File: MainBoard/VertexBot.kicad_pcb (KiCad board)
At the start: 2 copper layers, 115.6 x 107.8 mm, 68 parts, among them J2 I2C Extension, J3 Left Motor, J4 694106301002, J5 Right Motor, J6 Led Strip, Q1 BSS138, Q2 BSS138, Q3 BSS138, SW1 SW_SPST, U10 MAX4466 (LEFT), U11 MAX4466 (RIGHT), U12 ESP32-S3-CAM-B, U13 ESP32-S3-CAM-A, U14 MAX98357A, U2 DRV8830DGQR, U3 S13V30F5, U4 DRV8830DGQR, U5 INMP441, U6 0.96 INCH OLED, U7 DRV5033AJxLPG, U8 DRV5033AJxLPG, U9 MPU 6050

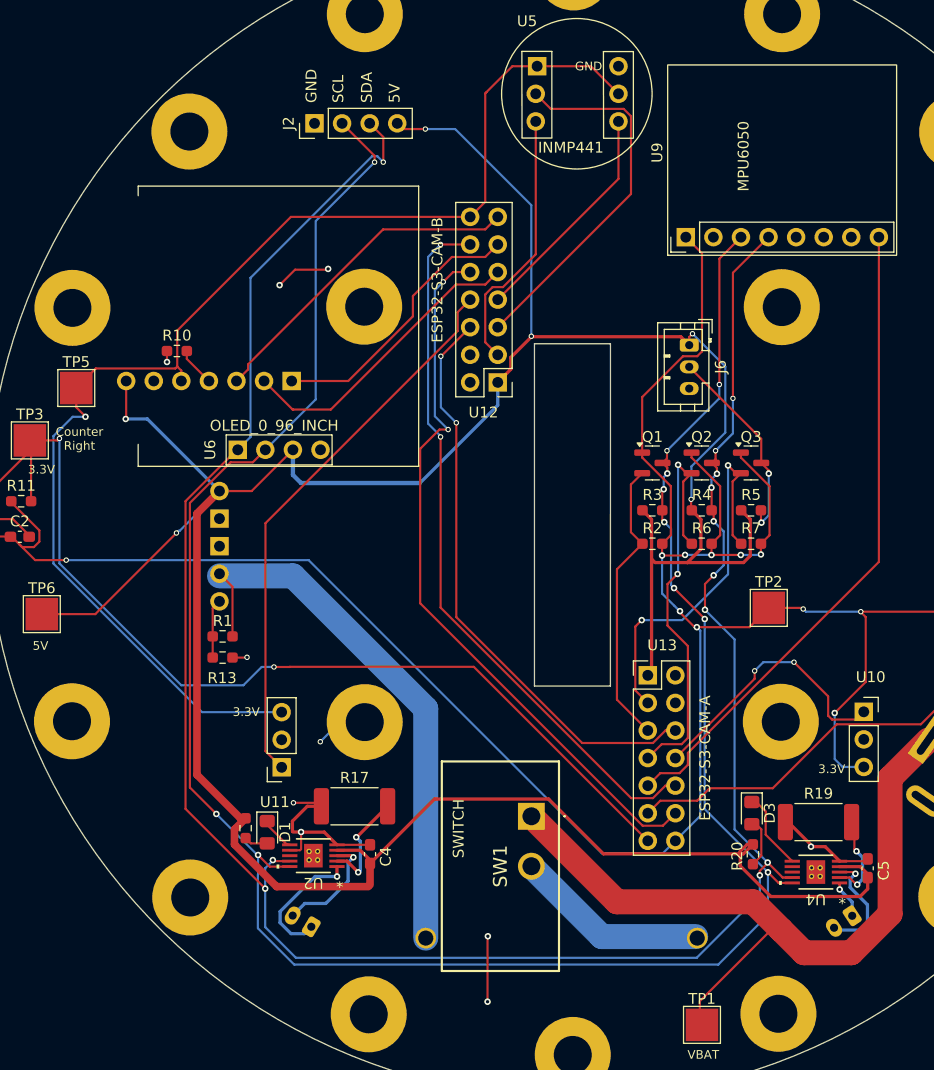
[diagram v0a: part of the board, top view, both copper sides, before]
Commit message: JLCPCB parts, refs, shops Corrected missing pins for backboard B
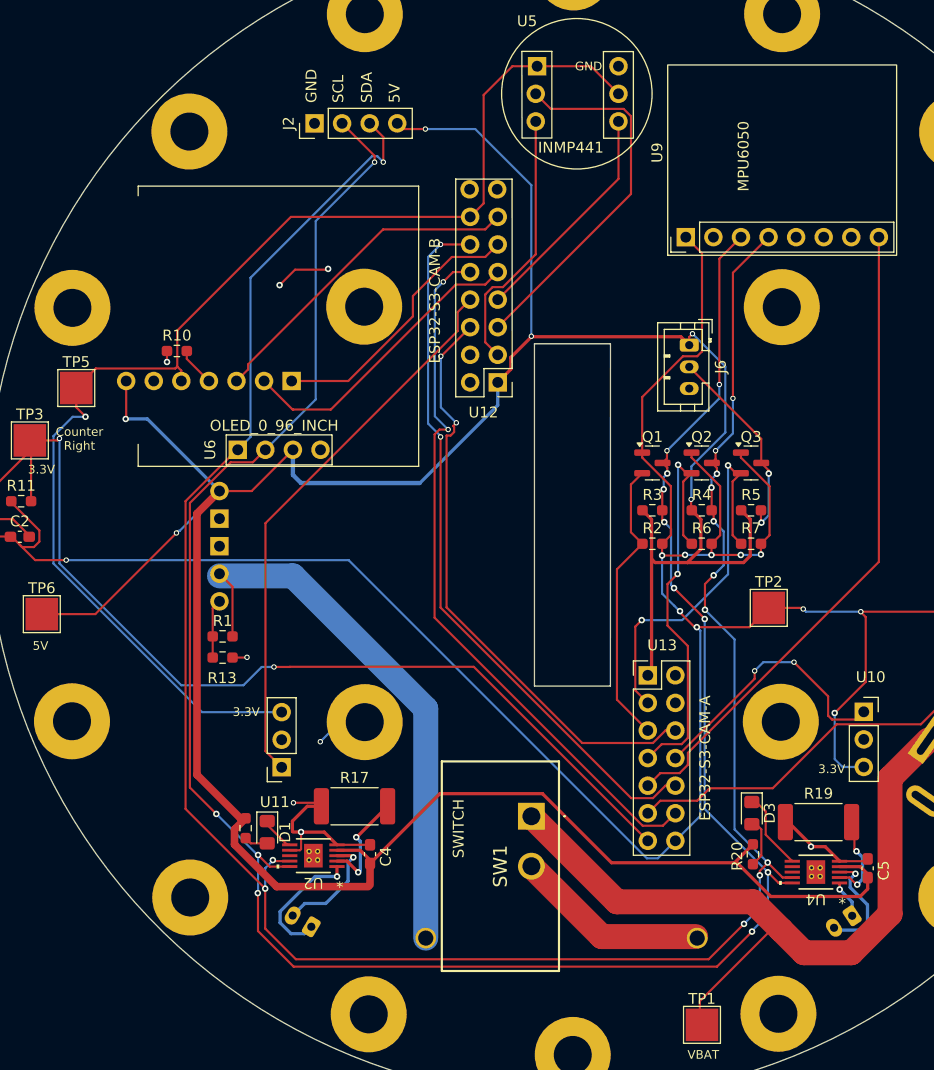
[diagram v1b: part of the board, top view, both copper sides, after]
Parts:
- C1, C2: value 10nf -> 100nf
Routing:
- net GND: track 55.9 -> 49.9 mm, vias 10 -> 8
- net TX: track 67.3 -> 66.2 mm
- net SYNC: track 53.9 -> 54.9 mm
- net SDA: track 210.0 -> 210.9 mm, vias 12 -> 13
- net SCL: track 212.3 -> 212.7 mm, vias 11 -> 13
